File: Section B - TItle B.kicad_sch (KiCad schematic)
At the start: 25 parts, among them J5 JST_SHBM04B-SRSS-TB, J6 Conn_02x07_Odd_Even, J7 THD-20-R, J8 THD-02-R, J9 Micro_SD_Card_Det, SW1 Right angle Tact button, U3 74LVC1G07SE-7, U4 TPD4EUSB30, U5 TPD4EUSB30, U6 RT9742GGJ5, U7 MagJack-A70-112-331N126

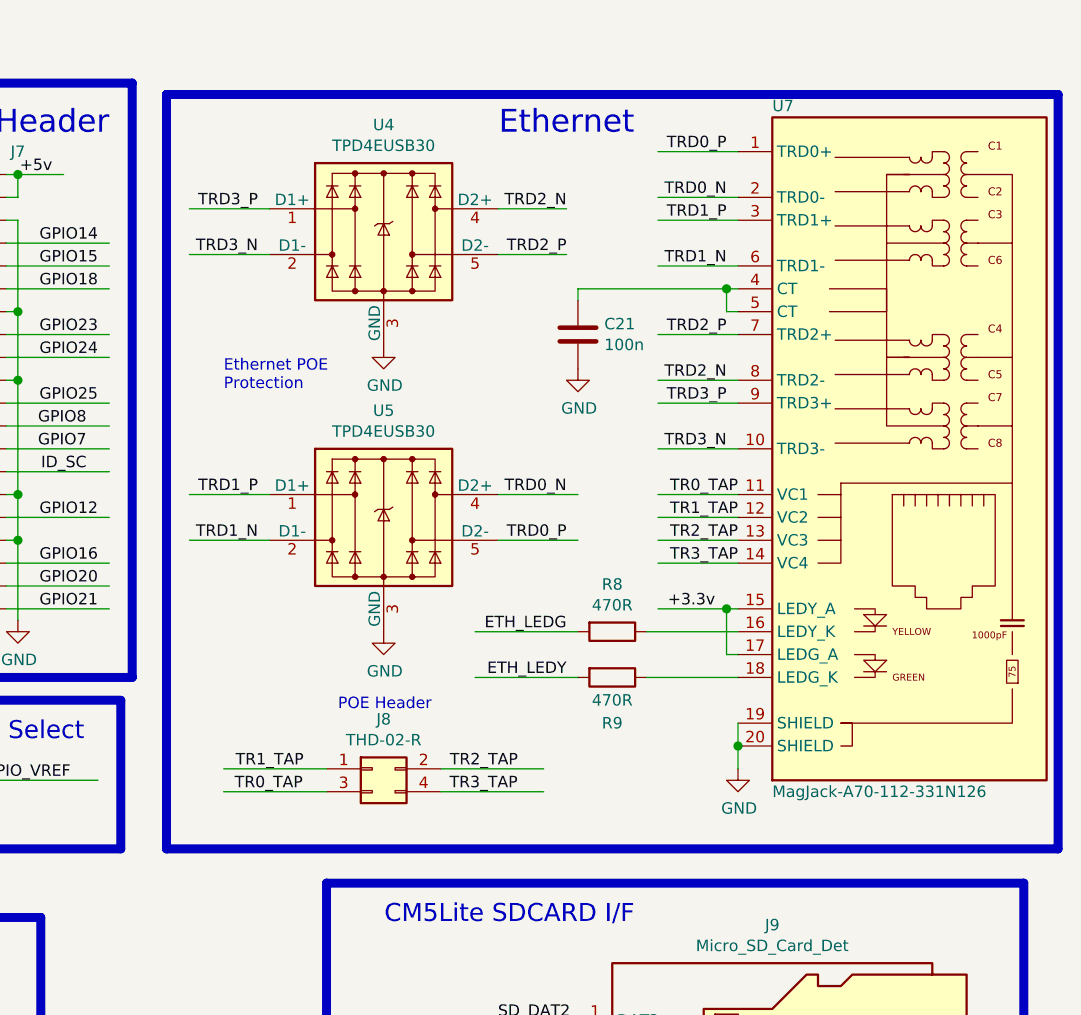
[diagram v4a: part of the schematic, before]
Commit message: Buck converter output voltage changed
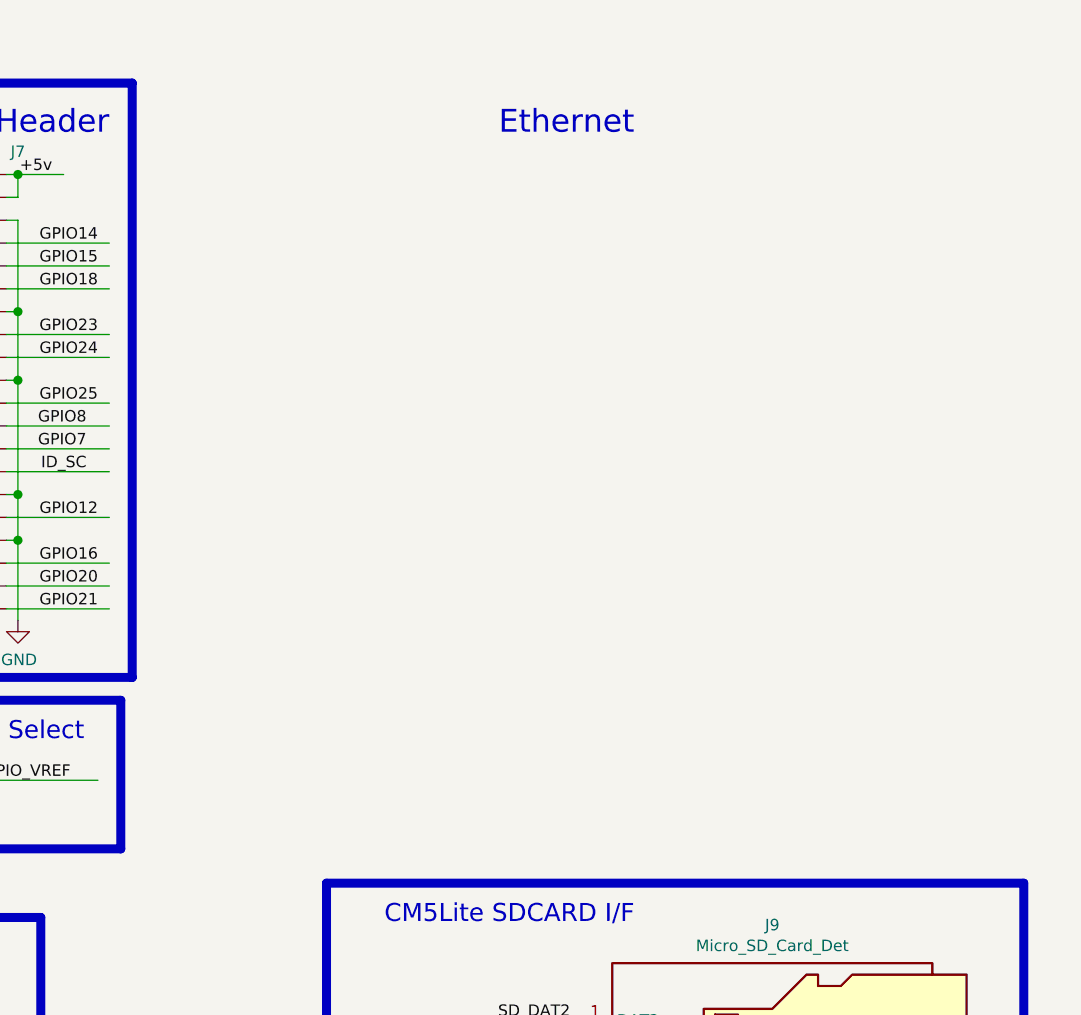
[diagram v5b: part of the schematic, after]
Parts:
- removed C21: 100n, Capacitor_SMD:C_0402_1005Metric, symbol Device:C
- removed J8: THD-02-R, Connector_PinHeader_2.54mm:PinHeader_2x02_P2.54mm_Vertical, symbol Connector_Generic:Conn_02x02_Odd_Even
- removed R8, R9: 470R, Resistor_SMD:R_0402_1005Metric, symbol Device:R
- removed U4, U5: TPD4EUSB30, Package_SON:USON-10_2.5x1.0mm_P0.5mm, symbol CM5IO:TPD4EUSB30
- removed U7: MagJack-A70-112-331N126, CM5IO:TRJG0926HENL, symbol CM5IO:MagJack-A70-112-331N126
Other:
- note removed: "Ethernet POE Protection"
- note removed: "POE Header"

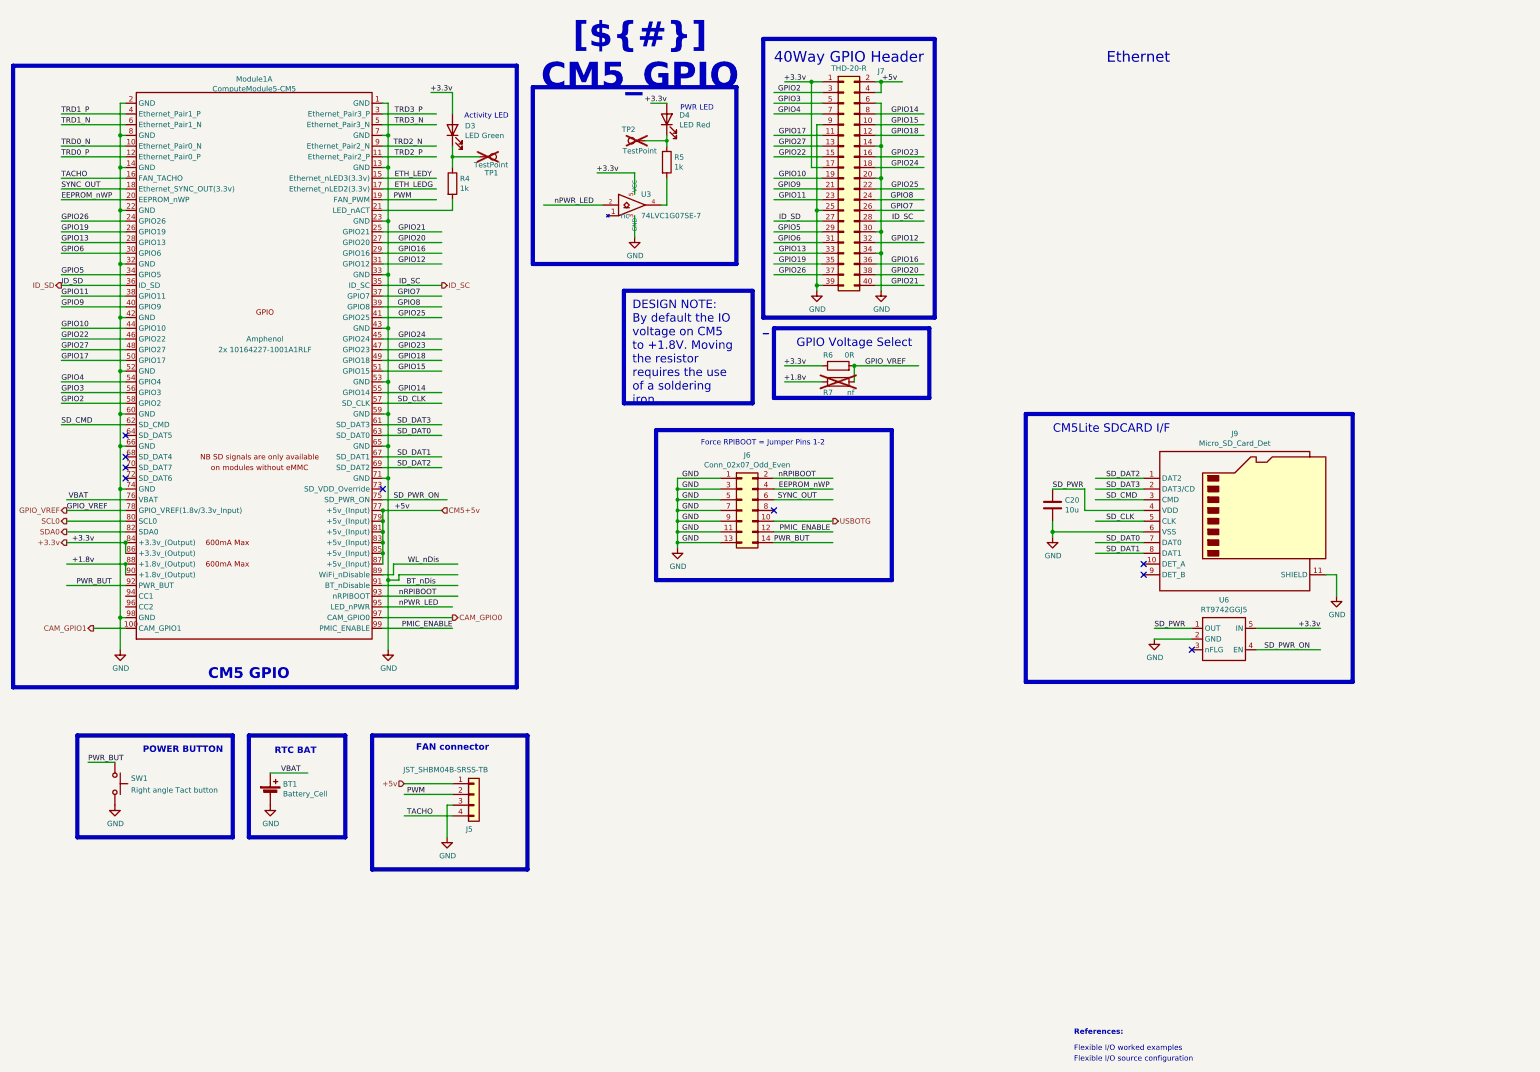
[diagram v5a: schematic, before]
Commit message: etherenet schematic
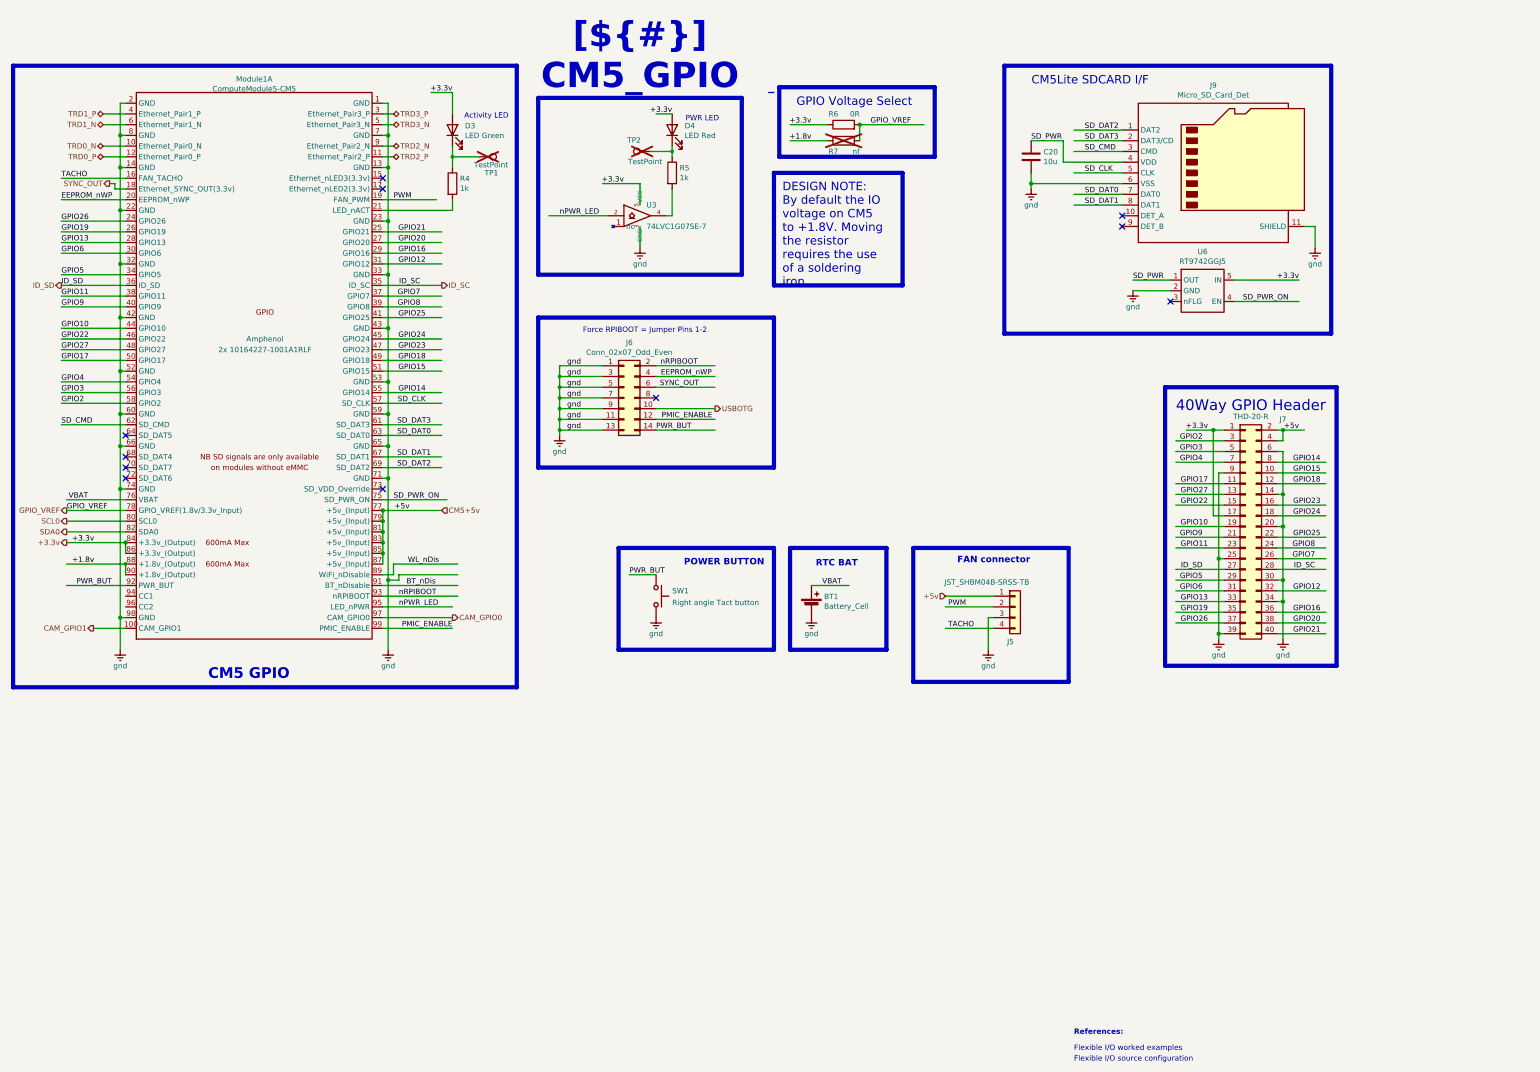
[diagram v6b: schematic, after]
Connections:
- net ETH_LEDG: no longer names the net of Module1.17 (Ethernet_nLED2(3.3v))
- net ETH_LEDY: no longer names the net of Module1.15 (Ethernet_nLED3(3.3v))
- net GND renamed gnd
- no-connect marks 9 -> 11
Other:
- moved on the sheet: BT1, C20, D4, J5, J6, J7, J9, R5, R6, R7, SW1, TP2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

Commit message: Swiitched to JSM561
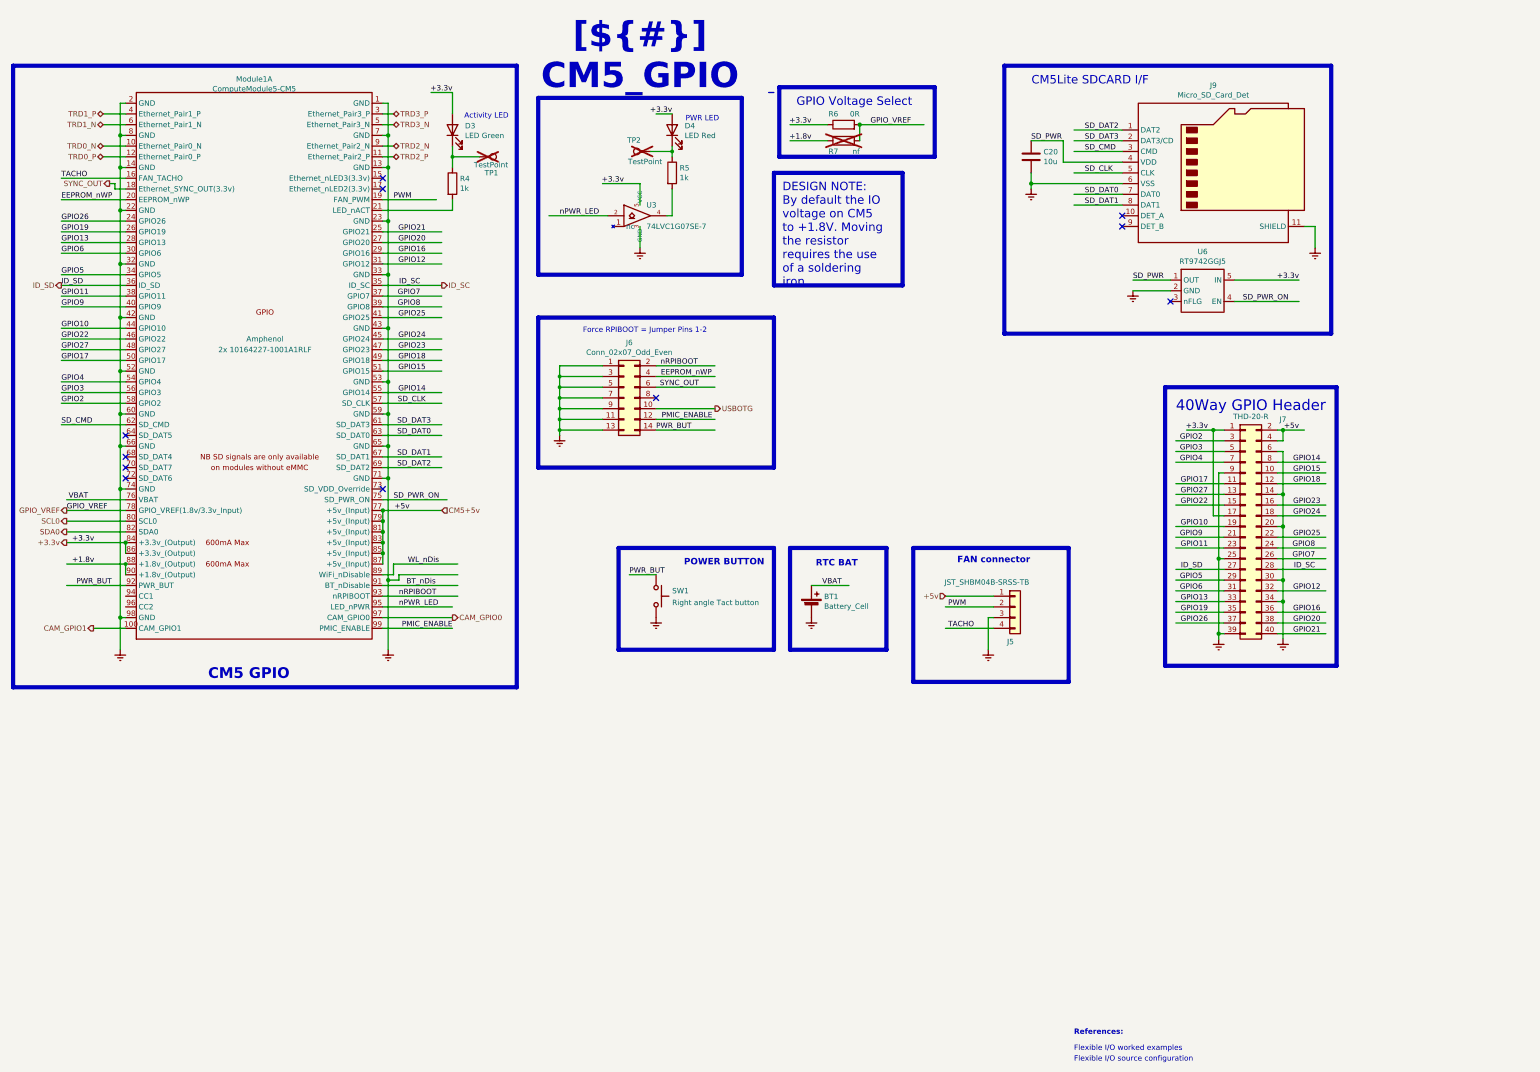
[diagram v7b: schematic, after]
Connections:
- removed net gnd: BT1.2 (-), C20.2, J5.3 (Pin_3), J6.1 (Pin_1), J6.11 (Pin_11), J6.13 (Pin_13), J6.3 (Pin_3), J6.5 (Pin_5), J6.7 (Pin_7), J6.9 (Pin_9), J7.14 (Pin_14), J7.20 (Pin_20), J7.25 (Pin_25), J7.30 (Pin_30), J7.34 (Pin_34), J7.39 (Pin_39), J7.6 (Pin_6), J7.9 (Pin_9), J9.11 (SHIELD), J9.6 (VSS), Module1.1 (GND), Module1.13 (GND), Module1.14 (GND), Module1.2 (GND), Module1.22 (GND), Module1.23 (GND), Module1.32 (GND), Module1.33 (GND), Module1.42 (GND), Module1.43 (GND), Module1.52 (GND), Module1.53 (GND), Module1.59 (GND), Module1.60 (GND), Module1.65 (GND), Module1.66 (GND), Module1.7 (GND), Module1.71 (GND), Module1.74 (GND), Module1.8 (GND), Module1.98 (GND), SW1.2, U3.3 (GND), U6.2 (GND)
- new net: J7.14 (Pin_14), J7.20 (Pin_20), J7.30 (Pin_30), J7.34 (Pin_34), J7.6 (Pin_6)
- new net: J7.25 (Pin_25), J7.39 (Pin_39), J7.9 (Pin_9)
- new net: C20.2, J9.6 (VSS)
- new net: J6.1 (Pin_1), J6.11 (Pin_11), J6.13 (Pin_13), J6.3 (Pin_3), J6.5 (Pin_5), J6.7 (Pin_7), J6.9 (Pin_9)
- new net: Module1.1 (GND), Module1.13 (GND), Module1.23 (GND), Module1.33 (GND), Module1.43 (GND), Module1.53 (GND), Module1.59 (GND), Module1.65 (GND), Module1.7 (GND), Module1.71 (GND)
- new net: Module1.14 (GND), Module1.2 (GND), Module1.22 (GND), Module1.32 (GND), Module1.42 (GND), Module1.52 (GND), Module1.60 (GND), Module1.66 (GND), Module1.74 (GND), Module1.8 (GND), Module1.98 (GND)
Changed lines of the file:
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@@
 		)
 	)
-	(label "gnd"
+	(label ""
 		(at 148.59 101.6 180)
 		(effects
@@
 		)
 	)
-	(label "gnd"
+	(label ""
 		(at 148.59 91.44 180)
 		(effects
@@
 		)
 	)
-	(label "gnd"
+	(label ""
 		(at 148.59 96.52 180)
 		(effects
@@
 		)
 	)
-	(label "gnd"
+	(label ""
 		(at 148.59 104.14 180)
 		(effects
@@
 		)
 	)
-	(label "gnd"
+	(label ""
 		(at 148.59 99.06 180)
 		(effects
@@
 		)
 	)
-	(label "gnd"
+	(label ""
 		(at 148.59 106.68 180)
 		(effects
@@
 		)
 	)
-	(label "gnd"
+	(label ""
 		(at 148.59 93.98 180)
 		(effects
@@
 			)
 		)
-		(property "Value" "gnd"
+		(property "Value" "~"
 			(at 279.4 77.47 0)
 			(effects
@@
 			)
 		)
-		(property "Value" "gnd"
+		(property "Value" "~"
 			(at 314.96 160.02 0)
 			(effects
@@
 			)
 		)
-		(property "Value" "gnd"
+		(property "Value" "~"
 			(at 299.72 160.02 0)
 			(effects
@@
 			)
 		)
-		(property "Value" "gnd"
+		(property "Value" "~"
 			(at 39.37 162.56 0)
 			(effects
@@
 			)
 		)
-		(property "Value" "gnd"
+		(property "Value" "~"
 			(at 102.87 162.56 0)
 			(effects
@@
 			)
 		)
-		(property "Value" "gnd"
+		(property "Value" "~"
 			(at 162.56 67.31 0)
 			(effects
@@
 			)
 		)
-		(property "Value" "gnd"
+		(property "Value" "~"
 			(at 255.27 53.34 0)
 			(effects
@@
 			)
 		)
-		(property "Value" "gnd"
+		(property "Value" "~"
 			(at 322.58 67.31 0)
 			(effects
@@
 			)
 		)
-		(property "Value" "gnd"
+		(property "Value" "~"
 			(at 143.51 111.76 0)
 			(effects
@@
 			)
 		)
-		(property "Value" "gnd"
+		(property "Value" "~"
 			(at 245.11 162.56 0)
 			(effects
@@
 			)
 		)
-		(property "Value" "gnd"
+		(property "Value" "~"
 			(at 203.2 154.94 0)
 			(effects
@@
 			)
 		)
-		(property "Value" "gnd"
+		(property "Value" "~"
 			(at 166.37 154.94 0)
 			(effects
